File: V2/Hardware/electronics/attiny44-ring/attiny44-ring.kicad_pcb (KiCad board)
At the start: 2 copper layers, 50 x 50 mm, 21 parts, among them J1 CHAIN_RING, J3 STEPPER_DRIVER_IN, J5 AVR_ISP_2X3, U1 ATtiny44A-SS

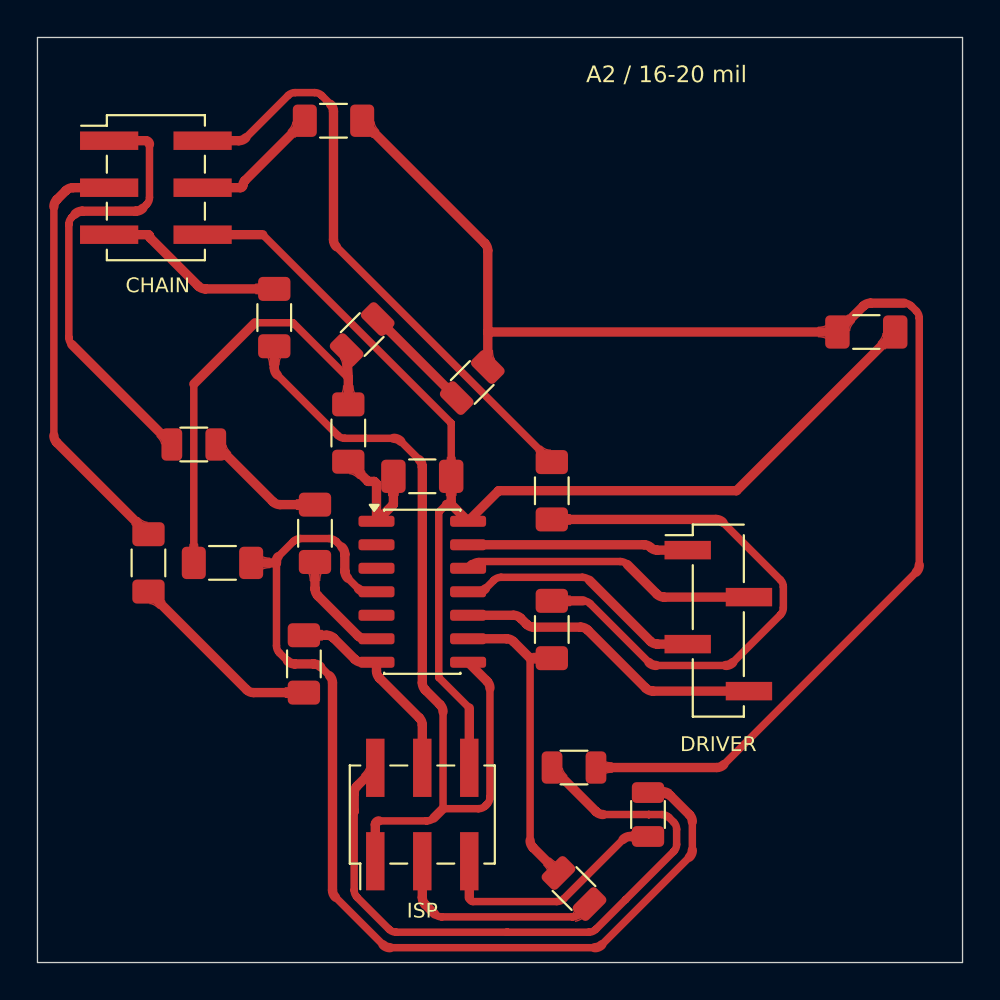
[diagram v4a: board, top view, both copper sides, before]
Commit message: Adapt organic trace radii and width tapers
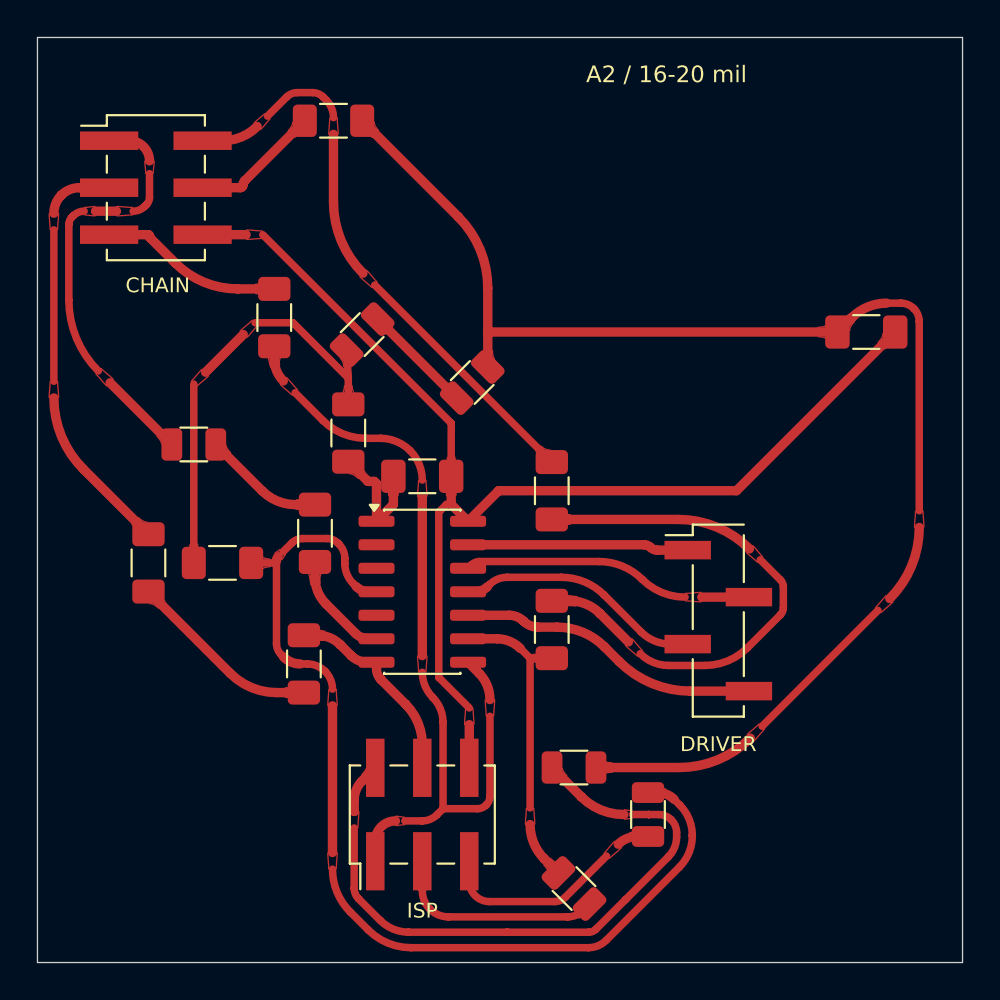
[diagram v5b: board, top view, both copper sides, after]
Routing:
- net DATA_OUT_A: track 47.0 -> 41.9 mm
- net LATCH_CONN: track 24.4 -> 20.7 mm
- net +5V_TOP: track 75.9 -> 72.3 mm
- net CLOCK_TOP: track 32.4 -> 29.4 mm
- net RESET: track 56.7 -> 53.8 mm
- net GND: track 66.0 -> 63.7 mm
- net CLOCK_A: track 30.5 -> 28.3 mm
- net DATA_CHAIN_IN: track 23.3 -> 21.2 mm
- net +5V: track 23.6 -> 21.8 mm
- net RESET_ISP: track 13.2 -> 11.4 mm
- net ISP_VCC: track 36.5 -> 34.8 mm
- net MOTOR2: track 16.0 -> 14.9 mm
- net CLOCK_U1: track 17.2 -> 16.1 mm
- net CLOCK_ISP: track 11.8 -> 11.1 mm
- net MOTOR3: track 13.6 -> 13.0 mm
